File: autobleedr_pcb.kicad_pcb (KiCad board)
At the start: 4 copper layers, 88.6 x 91 mm, 30 parts, among them J1 Barrel_Jack, J10 XT60 Connector, J11 Conn_01x02_Pin, J13 Screw_Terminal_01x08, J2 Conn_01x01_Pin, J4 Conn_01x13_Pin, J5 Conn_01x13_Pin, J7 Screw_Terminal_01x02, J8 Conn_01x02_Pin, J9 Conn_01x02_Pin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

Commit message: Made some changes for Barnes
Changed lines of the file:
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@@
 		(tags "Switch")
 		(property "Reference" "S1"
-			(at 1.672 -4.7 180)
+			(at 4.320098 -13.19995 180)
 			(layer "F.SilkS")
 			(effects
@@
 		)
 		(fp_text user "${REFERENCE}"
-			(at 1.672 -4.7 180)
+			(at 4.320098 -13.19995 180)
 			(layer "F.Fab")
 			(effects
@@
 		(tags "Resistor Axial_DIN0207 series Axial Horizontal pin pitch 7.62mm 0.25W = 1/4W length 6.3mm diameter 2.5mm")
 		(property "Reference" "R1"
-			(at 3.81 -2.2 90)
+			(at 9.93195 -0.152902 180)
 			(layer "F.SilkS")
 			(effects
@@
 		(tags "LED IR")
 		(property "Reference" "D2"
-			(at 5.29 -0.05 180)
+			(at -2.88195 -0.147098 180)
 			(layer "F.SilkS")
 			(effects
@@
 		(at 103.192 73.178)
 		(property "Reference" "U6"
-			(at 0.007902 -0.87805 0)
+			(at 14.657902 -10.27805 0)
 			(unlocked yes)
 			(layer "F.SilkS")

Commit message: updated v2
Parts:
- removed 1, 3: MountingHole_4.3mm_M4_ISO7380_Pad, MountingHole:MountingHole_4.3mm_M4_ISO7380_Pad
- removed J1: Barrel_Jack, Connector_BarrelJack:BarrelJack_CUI_PJ-063AH_Horizontal
- removed J10: XT60 Connector, Connector_AMASS:AMASS_XT60PW-F_1x02_P7.20mm_Horizontal
- removed J4, J5: Conn_01x13_Pin, Connector_PinHeader_2.54mm:PinHeader_1x13_P2.54mm_Vertical
- removed J8, J9: Conn_01x02_Pin, Connector_PinHeader_2.54mm:PinHeader_1x02_P2.54mm_Vertical
- removed S1: 7201SYCQE, Capstone_Footprints:7201SYCQE
- removed U4: Buck Converter, Capstone_Footprints:Buck_Converter
- moved J7 87.6 mm to (53.5, 148.7), turned to -90 degrees
- moved D2 75.5 mm to (53.8, 140.5)
- moved R4 74.2 mm to (51.3, 113.4)
- moved C1 73.5 mm to (56.6, 113.8)
- moved R1 62.6 mm to (56.2, 125.6)
- moved J2 49.2 mm to (88.6, 118.7)
- moved U2 48.4 mm to (60.8, 129.7)
- moved U6 48.2 mm to (73.0, 110.7)
- moved C3 46.5 mm to (83.9, 73.1)
- moved 2 45.4 mm to (87.8, 65.7)
- moved D1 39.3 mm to (55.1, 120.1)
- moved R2 34.9 mm to (52.2, 125.9), turned to -90 degrees
- moved 4 23.6 mm to (54.3, 171.1)
- moved J11 23.3 mm to (54.5, 159.3)
- moved C2 22.6 mm to (84.3, 93.2)
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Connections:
- C1 pad 1: 3V3 -> +3.3V
- C2 pad 1: +12V -> +7.4V
- C3 pad 1: +12V -> +7.4V
- ERMU7 pad 14: +12V -> +7.4V
- J11 pad 1: +12V -> +7.4V
- J7 pad 1: +12V -> +7.4V
- LinU1 pad 14: +12V -> +7.4V
- R2 pad 2: +12V -> +7.4V
- R4 pad 1: 3V3 -> +3.3V
- U2 pad 1: Net-(J4-Pin_1) -> unconnected-(U2-EN-Pad1)
- U2 pad 12: Net-(J4-Pin_12) -> unconnected-(U2-D12-Pad12)
- U2 pad 13: Net-(J4-Pin_13) -> unconnected-(U2-D13-Pad13)
- U2 pad 15: +3.3V -> +7.4V
- U2 pad 16: 3V3 -> +3.3V
- U2 pad 18: Net-(J5-Pin_13) -> unconnected-(U2-D15-Pad18)
- U2 pad 19: Net-(J5-Pin_12) -> unconnected-(U2-D2-Pad19)
- U2 pad 2: Net-(J4-Pin_2) -> unconnected-(U2-VP-Pad2)
- U2 pad 20: Net-(J5-Pin_11) -> unconnected-(U2-D4-Pad20)
- U2 pad 21: Net-(J5-Pin_10) -> unconnected-(U2-RX2-Pad21)
- U2 pad 22: Net-(J5-Pin_9) -> unconnected-(U2-TX2-Pad22)
- U2 pad 23: Net-(J5-Pin_8) -> unconnected-(U2-D5-Pad23)
- U2 pad 27: Net-(J5-Pin_4) -> unconnected-(U2-RX0-Pad27)
- U2 pad 28: Net-(J5-Pin_3) -> unconnected-(U2-TX0-Pad28)
- U2 pad 29: Net-(J5-Pin_2) -> unconnected-(U2-D22-Pad29)
- U2 pad 3: Net-(J4-Pin_3) -> unconnected-(U2-VN-Pad3)
- U2 pad 30: Net-(J5-Pin_1) -> unconnected-(U2-D23-Pad30)
- U2 pad 4: Net-(J4-Pin_4) -> unconnected-(U2-D34-Pad4)
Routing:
- net +12V: track 160.8 -> 0.00 mm
- net D35: track 95.4 -> 0.00 mm, vias 4 -> 0
- net +3.3V: track 92.7 -> 0.00 mm
- net /DIR: track 65.8 -> 0.00 mm
- net /enable DRV: track 63.3 -> 0.00 mm, vias 2 -> 0
- net /linear actuator direction: track 63.2 -> 0.00 mm, vias 2 -> 0
- net 3V3: track 62.7 -> 0.00 mm
- net /STEP: track 61.3 -> 0.00 mm
- net /DIAG: track 52.0 -> 0.00 mm
- net D32: track 51.6 -> 0.00 mm, vias 1 -> 0
- net /speed ERM DRV: track 38.3 -> 0.00 mm, vias 1 -> 0
- net /direction ERM DRV: track 35.0 -> 0.00 mm, vias 1 -> 0
- net /ERM vin: track 31.2 -> 0.00 mm
- net /ERM gnd: track 30.1 -> 0.00 mm
- net /enable ERM DRV: track 29.6 -> 0.00 mm, vias 1 -> 0
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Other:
- board size 88.6 x 91 mm -> 43.2 x 116.1 mm
- board text added: "AutoBleedr Version 2"
- board text added: "D33"
- board text removed: "12V"
- board text removed: "3V3"
- board text removed: "AutoBleedr Version 1"
- board text removed: "GND"
- board text removed: "Sel: Barrel Jack"

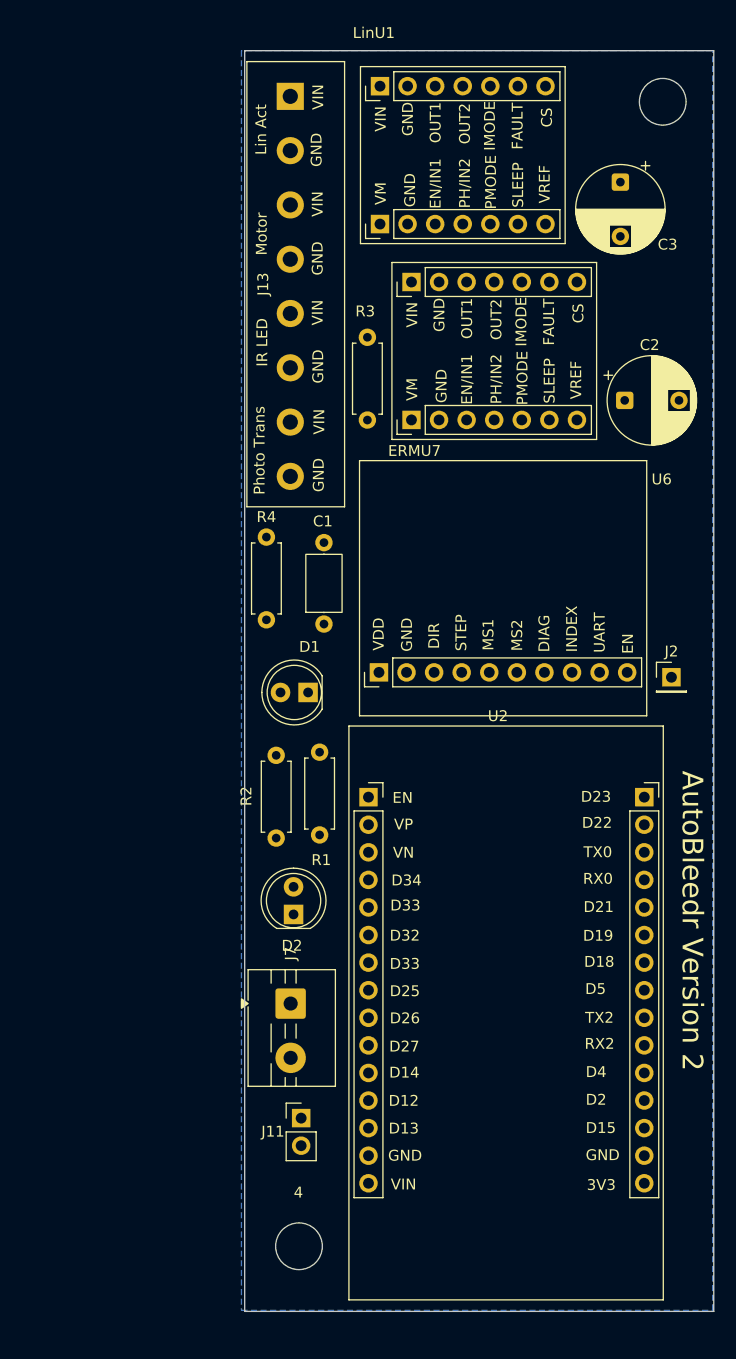
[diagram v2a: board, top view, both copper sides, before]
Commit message: updated board with new battery and v2 traces
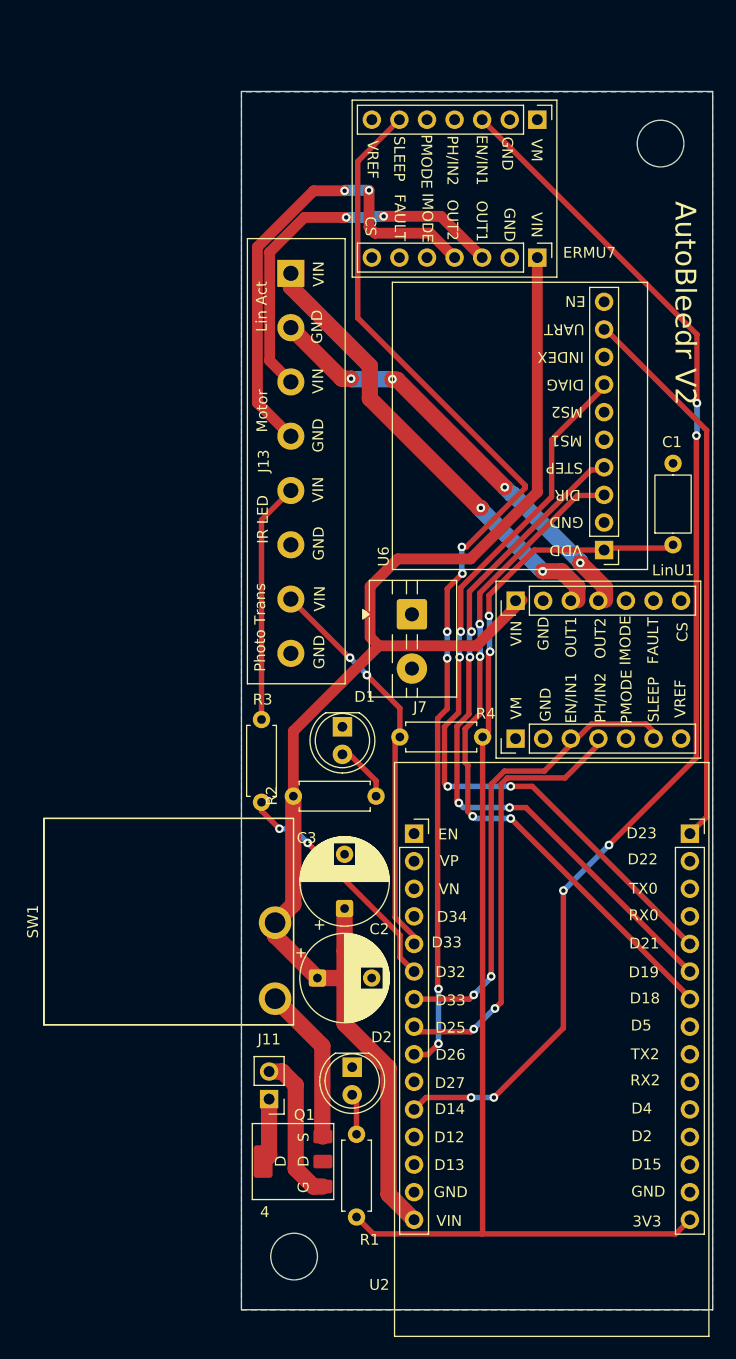
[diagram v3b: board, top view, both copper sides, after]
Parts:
- removed J2: Conn_01x01_Pin, Connector_PinHeader_2.54mm:PinHeader_1x01_P2.54mm_Vertical
- added Q1: PMOS, Capstone_Footprints:DMP6023LE, F.Cu at (53.5, 163.3)
- added SW1: SW_SPST, Capstone_Footprints:R1966ABLKBLKGR, F.Cu at (41.8, 141.2)
- moved C3 71.6 mm to (58.5, 140.0), turned to 90 degrees
- moved C2 60.3 mm to (56.0, 146.4)
- moved LinU1 49.0 mm to (72.4, 117.9)
- moved J7 37.5 mm to (64.7, 112.9)
- moved R3 36.5 mm to (50.8, 130.2)
- moved R1 35.4 mm to (59.6, 160.8)
- moved C1 33.0 mm to (88.7, 106.5)
- moved R4 22.6 mm to (71.2, 124.2), turned to 180 degrees
- moved ERMU7 21.2 mm to (78.0, 73.8), turned to -90 degrees
- moved J13 16.3 mm to (54.5, 98.8)
- moved U6 15.3 mm to (74.9, 95.6), turned to 90 degrees
- moved D2 15.1 mm to (59.2, 154.6), turned to -90 degrees
- moved R2 9.94 mm to (61.4, 129.6), turned to 180 degrees
- moved U2 5.38 mm to (65.0, 133.1)
- moved D1 4.47 mm to (58.3, 123.3), turned to -90 degrees
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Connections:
- C2 pad 1: +7.4V -> +7.5V
- C3 pad 1: +7.4V -> +7.5V
- ERMU7 pad 14: +7.4V -> +7.5V
- J11 pad 1: +7.4V -> /Battery+
- J11 pad 2: GND -> /Battery-
- J7 pad 1: +7.4V -> /Stp Mtr Power Wire
- LinU1 pad 14: +7.4V -> +7.5V
- R2 pad 2: +7.4V -> +7.5V
- U2 pad 15: +7.4V -> +7.5V
- U2 pad 30: unconnected-(U2-D23-Pad30) -> /TMC UART
- U6 pad 9: Net-(J2-Pin_1) -> /TMC UART
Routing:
- net +7.5V: track 0.00 -> 131.3 mm
- net /speed ERM DRV: track 0.00 -> 113.8 mm, vias 0 -> 6
- net +3.3V: track 0.00 -> 109.9 mm, vias 0 -> 2
- net /enable ERM DRV: track 0.00 -> 99.4 mm, vias 0 -> 6
- net /DIAG: track 0.00 -> 71.6 mm, vias 0 -> 4
- net /STEP: track 0.00 -> 65.3 mm, vias 0 -> 4
- net /DIR: track 0.00 -> 63.7 mm, vias 0 -> 4
- net /TMC UART: track 0.00 -> 51.1 mm
- net /enable DRV: track 0.00 -> 44.1 mm, vias 0 -> 2
- net /ERM gnd: track 0.00 -> 43.6 mm, vias 0 -> 2
- net /LIN ACT VIN: track 0.00 -> 42.1 mm, vias 0 -> 2
- net /linear actuator direction: track 0.00 -> 40.8 mm, vias 0 -> 2
- net /LIN ACT GND: track 0.00 -> 40.1 mm, vias 0 -> 4
- net D35: track 0.00 -> 36.9 mm, vias 0 -> 2
- net /ERM vin: track 0.00 -> 35.3 mm, vias 0 -> 2
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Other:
- board size 43.2 x 116.1 mm -> 43.4 x 112.2 mm
- board text added: "AutoBleedr V2"
- board text removed: "AutoBleedr Version 2"

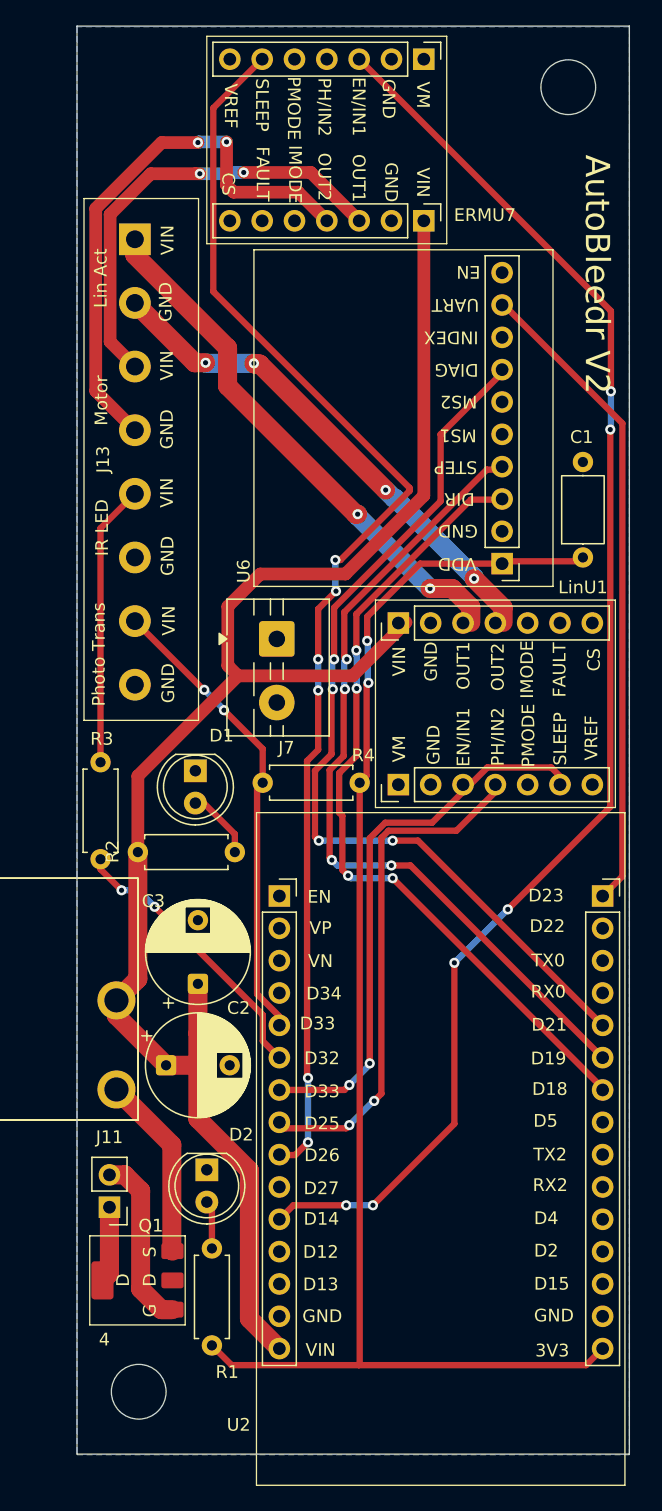
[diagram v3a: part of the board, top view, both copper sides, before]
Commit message: updated pcb traces with binh nmos design
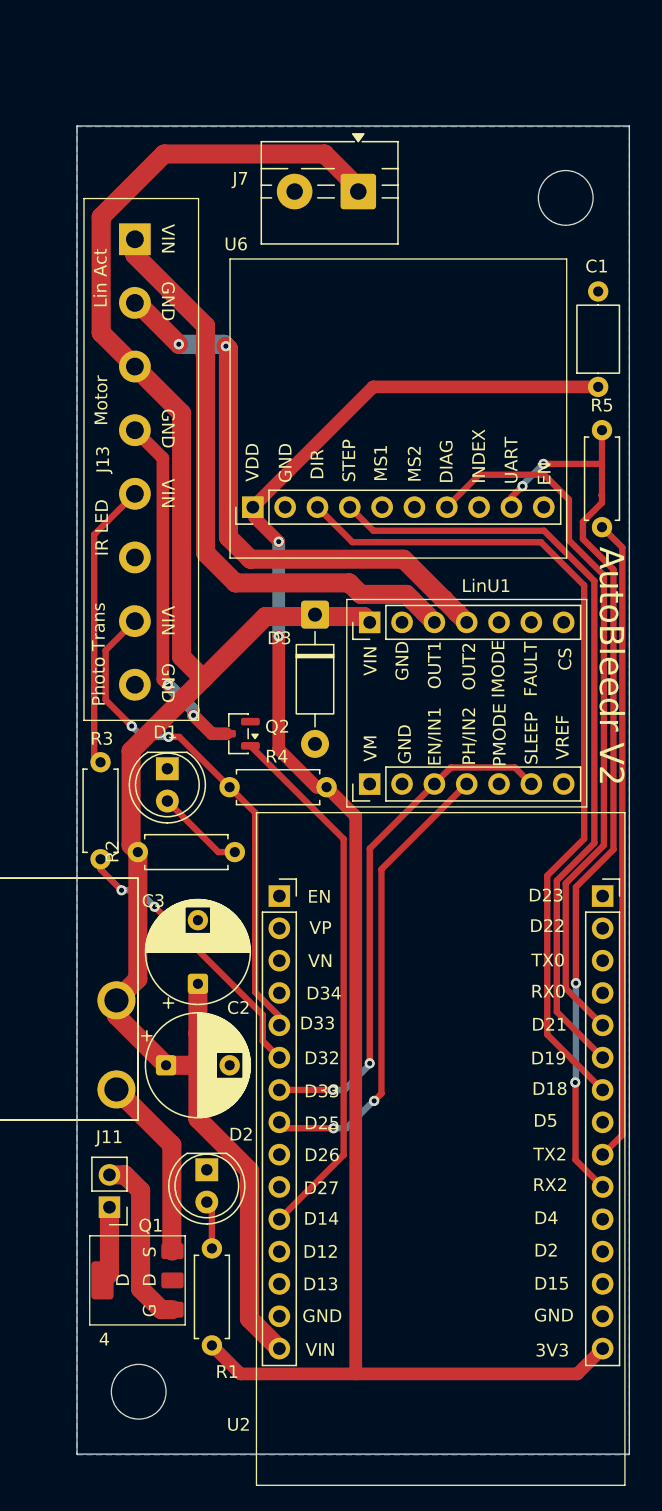
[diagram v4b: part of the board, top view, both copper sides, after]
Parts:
- removed ERMU7: DVR8874, Capstone_Footprints:DVR8874
- added D3: 1N4001, Diode_THT:D_DO-41_SOD81_P10.16mm_Horizontal, F.Cu at (67.7, 111.0)
- added Q2: IRLML2060, Package_TO_SOT_SMD:SOT-23, F.Cu at (61.7, 120.3)
- added R5: 1500R, Resistor_THT:R_Axial_DIN0207_L6.3mm_D2.5mm_P7.62mm_Horizontal, F.Cu at (90.2, 104.1)
- moved J7 35.7 mm to (71.1, 77.7), turned to 180 degrees
- moved C1 13.5 mm to (89.9, 93.1)
- moved 2 8.70 mm to (87.4, 78.2)
- moved R4 2.62 mm to (68.6, 124.5)
- moved LinU1 2.25 mm to (70.2, 117.8)
- moved D1 2.21 mm to (56.1, 123.1)
- moved U6 0.90 mm to (74.2, 95.0), turned to 0 degrees
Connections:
- J13 pad 3: /ERM vin -> +7.5V
- J13 pad 4: /ERM gnd -> /ERM neg
- J7 pad 1: /Stp Mtr Power Wire -> +7.5V
- U2 pad 21: unconnected-(U2-RX2-Pad21) -> /TMC UART
- U2 pad 22: unconnected-(U2-TX2-Pad22) -> Net-(U2-TX2)
- U2 pad 30: /TMC UART -> unconnected-(U2-D23-Pad30)
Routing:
- net /enable ERM DRV: track 99.4 -> 0.04 mm, vias 6 -> 0
- net /speed ERM DRV: track 113.8 -> 42.3 mm, vias 6 -> 0
- net Net-(U2-TX2): track 0.00 -> 50.6 mm
- net /ERM gnd: track 43.6 -> 0.00 mm, vias 2 -> 0
- net /ERM vin: track 35.3 -> 0.00 mm, vias 2 -> 0
- net /ERM neg: track 0.00 -> 27.5 mm, vias 0 -> 2
- net +3.3V: track 109.9 -> 135.4 mm
- net /TMC UART: track 51.1 -> 72.7 mm, vias 0 -> 4
- net +7.5V: track 131.3 -> 147.9 mm
- net /DIAG: track 71.6 -> 56.4 mm, vias 4 -> 0
- net /LIN ACT GND: track 40.1 -> 45.1 mm, vias 4 -> 2
- net /LIN ACT VIN: track 42.1 -> 47.2 mm, vias 2 -> 0
- net /linear actuator direction: track 40.8 -> 36.4 mm
- net /STEP: track 65.3 -> 61.8 mm, vias 4 -> 0
- net /enable DRV: track 44.1 -> 40.8 mm
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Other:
- board size 43.4 x 112.2 mm -> 43.4 x 104.3 mm
- board text added: "VIN"
